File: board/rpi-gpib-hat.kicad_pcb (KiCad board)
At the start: 2 copper layers, 65 x 30 mm, 7 parts, among them J1 RPI_GPIO, J2 GPIB

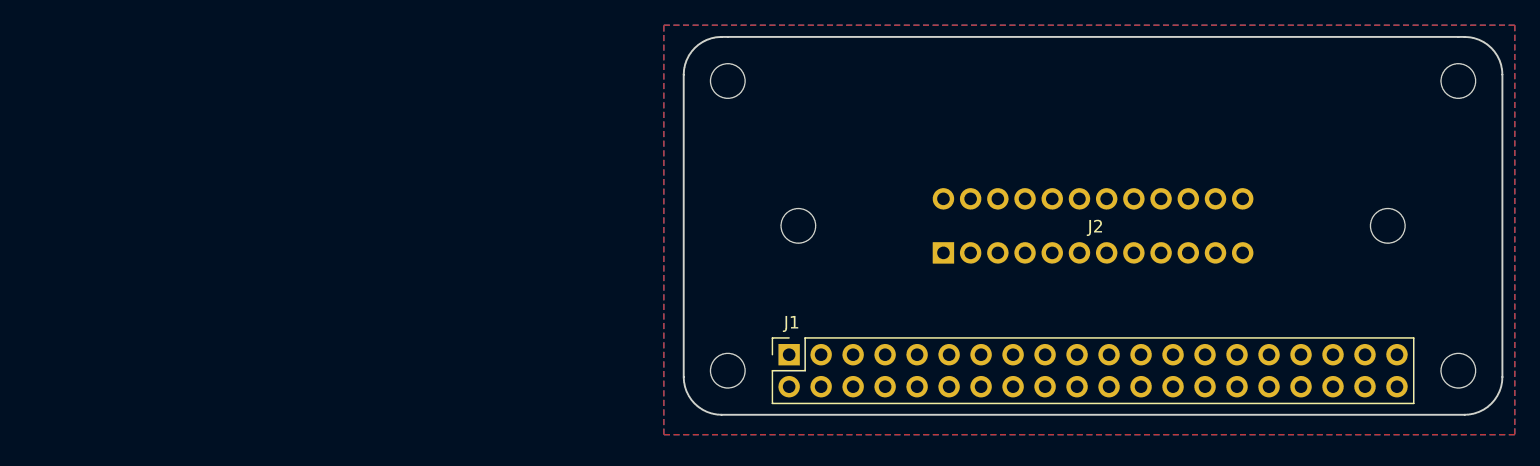
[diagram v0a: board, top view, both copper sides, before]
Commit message: Remove ground fills for now.
They're just in the way and there probably wont' be room for them.
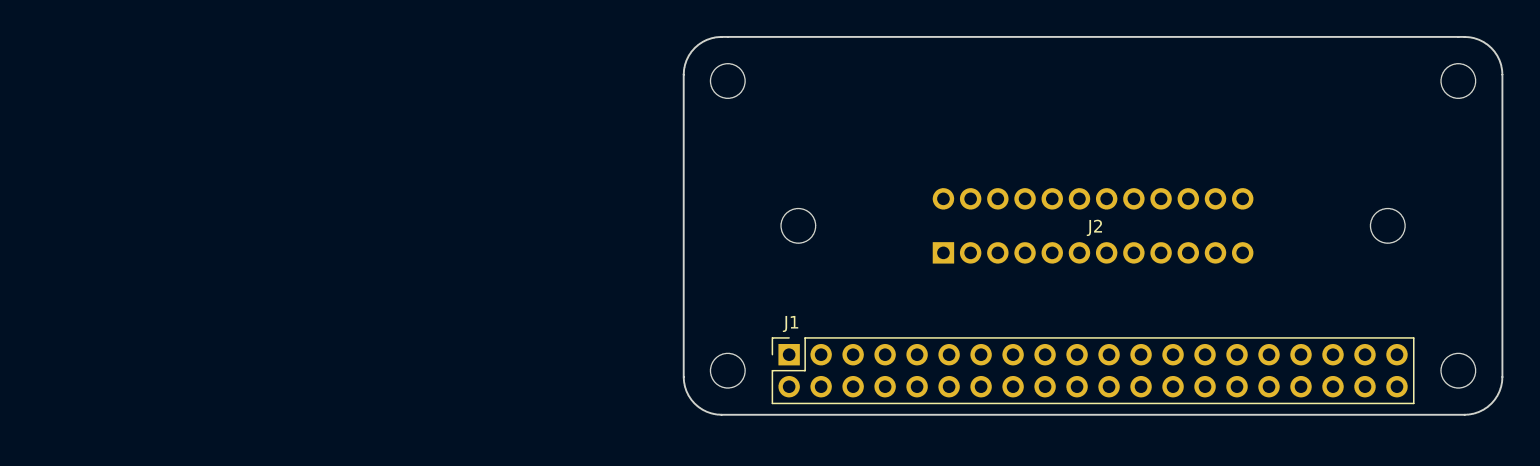
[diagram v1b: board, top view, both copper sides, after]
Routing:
- removed copper zone on B.Cu, net GND
- removed copper zone on F.Cu, net GND
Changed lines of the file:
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@@
   (gr_arc (start 158.5 123.5) (end 161.5 123.5) (angle 90) (layer Edge.Cuts) (width 0.15))
   (gr_line (start 100 96.5) (end 158 96.5) (layer Edge.Cuts) (width 0.15))
-  (zone (net 3) (net_name GND) (layer F.Cu) (hatch edge 0.508)
-    (connect_pads (clearance 0.508))
-    (min_thickness 0.254)
-    (fill yes (arc_segments 16) (thermal_gap 0.508) (thermal_bridge_width 0.508))
-    (polygon
-      (pts
-        (xy 94.92 128.08) (xy 94.92 95.568) (xy 162.484 95.568) (xy 162.484 128.08)
-      )
-    )
-  )
-  (zone (net 3) (net_name GND) (layer B.Cu) (hatch edge 0.508)
-    (connect_pads (clearance 0.508))
-    (min_thickness 0.254)
-    (fill yes (arc_segments 16) (thermal_gap 0.508) (thermal_bridge_width 0.508))
-    (polygon
-      (pts
-        (xy 94.92 128.08) (xy 94.92 95.568) (xy 162.484 95.568) (xy 162.484 128.08)
-      )
-    )
-  )
 )

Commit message: Start laying out the PCB.
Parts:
- added C1: 1u, Capacitor_SMD:C_0805_2012Metric, F.Cu at (71.8, 114.9)
- added C2: 1u, Capacitor_SMD:C_0805_2012Metric, F.Cu at (50.1, 124.9)
- added C3: 1u, Capacitor_SMD:C_0805_2012Metric, F.Cu at (58.6, 115.8)
- added D1: BAT54C, Package_TO_SOT_SMD:SOT-23, F.Cu at (98.8, 117.0)
- added D2: BAT54C, Package_TO_SOT_SMD:SOT-23, F.Cu at (98.8, 113.2)
- added D3: BAT54C, Package_TO_SOT_SMD:SOT-23, F.Cu at (98.8, 109.5)
- added D4: BAT54C, Package_TO_SOT_SMD:SOT-23, F.Cu at (98.8, 105.8)
- added D5: BAT54C, Package_TO_SOT_SMD:SOT-23, F.Cu at (45.7, 125.7)
- added D6: BAT54C, Package_TO_SOT_SMD:SOT-23, F.Cu at (54.1, 116.6)
- added D7: BAT54C, Package_TO_SOT_SMD:SOT-23, F.Cu at (71.5, 102.3)
- added D8: BAT54C, Package_TO_SOT_SMD:SOT-23, F.Cu at (54.1, 121.2)
- added R1: 3k, Resistor_SMD:R_0402_1005Metric, F.Cu at (50.1, 127.9)
- added R10: 3k, Resistor_SMD:R_0402_1005Metric, F.Cu at (80.3, 104.4)
- added R11: 3k, Resistor_SMD:R_0402_1005Metric, F.Cu at (67.4, 116.5)
- added R12: 3k, Resistor_SMD:R_0402_1005Metric, F.Cu at (63.0, 121.7)
- added R13: 3k, Resistor_SMD:R_0402_1005Metric, F.Cu at (75.9, 107.4)
- added R14: 3k, Resistor_SMD:R_0402_1005Metric, F.Cu at (75.9, 101.5)
- added R15: 3k, Resistor_SMD:R_0402_1005Metric, F.Cu at (80.3, 101.5)
- added R16: 3k, Resistor_SMD:R_0402_1005Metric, F.Cu at (54.5, 127.9)
- added R17: 6k2, Resistor_SMD:R_0402_1005Metric, F.Cu at (67.4, 113.5)
- added R18: 6k2, Resistor_SMD:R_0402_1005Metric, F.Cu at (58.6, 121.7)
- added R19: 6k2, Resistor_SMD:R_0402_1005Metric, F.Cu at (71.5, 109.0)
- added R2: 3k, Resistor_SMD:R_0402_1005Metric, F.Cu at (58.6, 118.8)
- added R20: 6k2, Resistor_SMD:R_0402_1005Metric, F.Cu at (75.9, 104.4)
- added R21: 6k2, Resistor_SMD:R_0402_1005Metric, F.Cu at (63.0, 118.8)
- added R22: 6k2, Resistor_SMD:R_0402_1005Metric, F.Cu at (58.9, 124.7)
- added R23: 6k2, Resistor_SMD:R_0402_1005Metric, F.Cu at (72.2, 120.8)
- added R24: 6k2, Resistor_SMD:R_0402_1005Metric, F.Cu at (84.7, 101.5)
- added R25: 6k2, Resistor_SMD:R_0402_1005Metric, F.Cu at (76.2, 116.2)
- added R26: 6k2, Resistor_SMD:R_0402_1005Metric, F.Cu at (67.7, 125.3)
- added R27: 6k2, Resistor_SMD:R_0402_1005Metric, F.Cu at (89.2, 104.4)
- added R28: 6k2, Resistor_SMD:R_0402_1005Metric, F.Cu at (84.7, 107.4)
- added R29: 6k2, Resistor_SMD:R_0402_1005Metric, F.Cu at (67.7, 122.4)
- added R3: 3k, Resistor_SMD:R_0402_1005Metric, F.Cu at (71.5, 106.0)
- added R30: 6k2, Resistor_SMD:R_0402_1005Metric, F.Cu at (71.8, 117.8)
- added R31: 6k2, Resistor_SMD:R_0402_1005Metric, F.Cu at (54.5, 124.9)
- added R32: 6k2, Resistor_SMD:R_0402_1005Metric, F.Cu at (80.6, 110.3)
- added R33: 500R, Resistor_SMD:R_0402_1005Metric, F.Cu at (101.8, 115.4)
- added R34: 500R, Resistor_SMD:R_0402_1005Metric, F.Cu at (101.8, 114.2)
- added R35: 500R, Resistor_SMD:R_0402_1005Metric, F.Cu at (101.8, 112.9)
- added R36: 500R, Resistor_SMD:R_0402_1005Metric, F.Cu at (101.8, 111.6)
- added R37: 500R, Resistor_SMD:R_0402_1005Metric, F.Cu at (101.8, 110.4)
- added R38: 500R, Resistor_SMD:R_0402_1005Metric, F.Cu at (101.8, 109.1)
- added R39: 500R, Resistor_SMD:R_0402_1005Metric, F.Cu at (101.8, 107.8)
- added R4: 3k, Resistor_SMD:R_0402_1005Metric, F.Cu at (67.0, 110.6)
- added R40: 500R, Resistor_SMD:R_0402_1005Metric, F.Cu at (101.8, 106.6)
- added R41: 500R, Resistor_SMD:R_0402_1005Metric, F.Cu at (85.0, 110.3)
- added R42: 500R, Resistor_SMD:R_0402_1005Metric, F.Cu at (89.1, 107.4)
- added R43: 500R, Resistor_SMD:R_0402_1005Metric, F.Cu at (72.2, 123.7)
- added R44: 500R, Resistor_SMD:R_0402_1005Metric, F.Cu at (67.7, 128.3)
- added R45: 500R, Resistor_SMD:R_0402_1005Metric, F.Cu at (76.6, 119.2)
- added R46: 500R, Resistor_SMD:R_0402_1005Metric, F.Cu at (80.6, 116.2)
- added R47: 500R, Resistor_SMD:R_0402_1005Metric, F.Cu at (85.0, 113.3)
- added R48: 500R, Resistor_SMD:R_0402_1005Metric, F.Cu at (89.4, 110.3)
- added R49: 3k9, Resistor_SMD:R_0402_1005Metric, F.Cu at (76.6, 122.1)
- added R5: 3k, Resistor_SMD:R_0402_1005Metric, F.Cu at (80.6, 113.3)
- added R50: 3k9, Resistor_SMD:R_0402_1005Metric, F.Cu at (72.2, 126.7)
- added R51: 1k, Resistor_SMD:R_0402_1005Metric, F.Cu at (81.0, 119.2)
- added R6: 3k, Resistor_SMD:R_0402_1005Metric, F.Cu at (85.0, 116.2)
- added R7: 3k, Resistor_SMD:R_0402_1005Metric, F.Cu at (63.0, 115.8)
- added R8: 3k, Resistor_SMD:R_0402_1005Metric, F.Cu at (58.9, 127.6)
- added R9: 3k, Resistor_SMD:R_0402_1005Metric, F.Cu at (71.8, 111.9)
- added TP1: TestPoint, TestPoint:TestPoint_Pad_D1.0mm, F.Cu at (88.8, 113.3)
- added U1: SN75162BDW, Package_SO:SOIC-24W_7.5x15.4mm_P1.27mm, F.Cu at (149.0, 111.0)
- added U2: SN75160BDW, Package_SO:SOIC-20W_7.5x12.8mm_P1.27mm, F.Cu at (109.0, 111.0)
- added U3: CAT24C32, Package_SO:SOIC-8_3.9x4.9mm_P1.27mm, F.Cu at (128.2, 101.5)
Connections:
- J1 pad 23: /GPIO11 -> (no net)
- J1 pad 29: /GPIO5 -> (no net)
- J1 pad 31: /GPIO6 -> (no net)
- J1 pad 36: /GPIO16 -> (no net)
- J1 pad 8: /GPIO14 -> (no net)
- J2 pad 12: Earth_Clean -> (no net)
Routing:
- net +3V3: track 0.00 -> 21.9 mm
- net /DAV: track 0.00 -> 19.9 mm, vias 0 -> 1
- net /REN: track 0.00 -> 19.7 mm
- net /EOI: track 0.00 -> 19.2 mm
- net /NRFD: track 0.00 -> 18.1 mm, vias 0 -> 1
- net /NDAC: track 0.00 -> 16.5 mm, vias 0 -> 1
- net /IFC: track 0.00 -> 15.1 mm, vias 0 -> 1
- net /DIO8: track 0.00 -> 11.1 mm
- net /DIO4: track 0.00 -> 10.8 mm
- net /DIO3: track 0.00 -> 8.85 mm
- net /SRQ: track 0.00 -> 8.54 mm
- net /DIO7: track 0.00 -> 8.42 mm
- net /DIO2: track 0.00 -> 7.46 mm
- net /ATN: track 0.00 -> 6.53 mm
- net /DIO6: track 0.00 -> 6.44 mm
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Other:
- net class Power added: clearance 0.1524, trace_width 0.3048, via_dia 0.508, via_drill 0.254

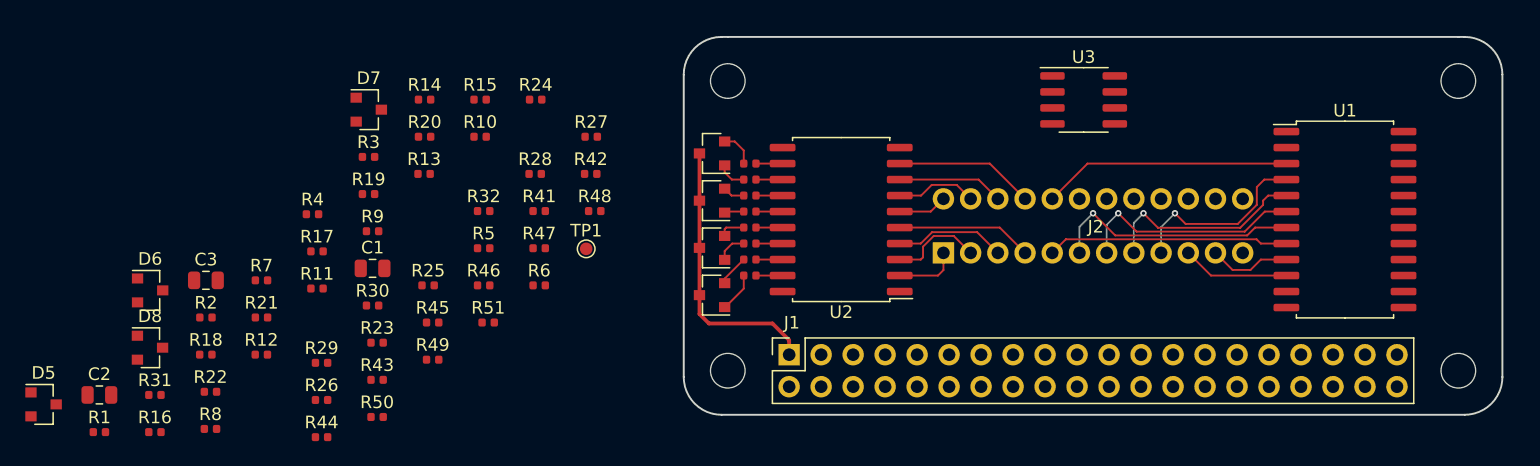
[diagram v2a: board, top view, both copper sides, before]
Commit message: Finish routing terminal-side GPIB lines.
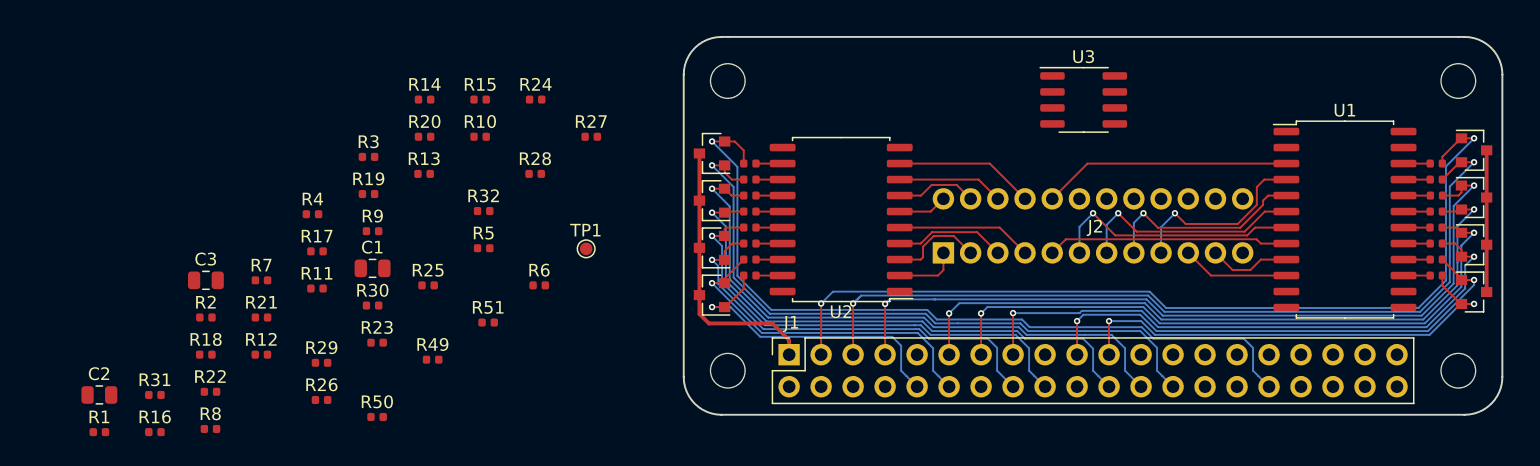
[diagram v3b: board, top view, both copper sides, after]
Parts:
- moved D5 115.4 mm to (159.2, 105.5)
- moved D6 105.4 mm to (159.2, 109.2)
- moved D8 105.2 mm to (159.2, 116.8)
- moved R44 90.3 mm to (156.2, 110.4)
- moved D7 88.4 mm to (159.2, 113.0)
- moved R43 85.4 mm to (156.3, 109.1)
- moved R45 80.0 mm to (156.2, 111.6)
- moved R46 75.7 mm to (156.2, 112.9)
- moved R41 71.3 mm to (156.2, 106.6)
- moved R47 71.2 mm to (156.2, 114.2)
- moved R42 67.1 mm to (156.2, 107.8)
- moved R48 67.0 mm to (156.2, 115.4)
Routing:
- net /GPIO2: track 0.00 -> 71.4 mm, vias 0 -> 2
- net /GPIO3: track 0.00 -> 67.0 mm, vias 0 -> 2
- net /GPIO4: track 0.00 -> 62.6 mm, vias 0 -> 2
- net /GPIO12: track 2.85 -> 62.3 mm, vias 0 -> 1
- net /GPIO17: track 0.00 -> 54.8 mm, vias 0 -> 2
- net /GPIO27: track 0.00 -> 50.8 mm, vias 0 -> 2
- net /GPIO7: track 2.30 -> 52.5 mm, vias 0 -> 1
- net /GPIO22: track 0.00 -> 47.2 mm, vias 0 -> 2
- net /GPIO8: track 1.74 -> 47.7 mm, vias 0 -> 1
- net /GPIO25: track 1.55 -> 43.3 mm, vias 0 -> 1
- net /GPIO10: track 0.00 -> 40.1 mm, vias 0 -> 2
- net /GPIO9: track 0.00 -> 37.0 mm, vias 0 -> 2
- net /GPIO24: track 2.11 -> 37.2 mm, vias 0 -> 1
- net /GPIO23: track 2.46 -> 33.4 mm, vias 0 -> 1
- net /GPIO18: track 2.50 -> 26.7 mm, vias 0 -> 1
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
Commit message: Route data bus terminators.
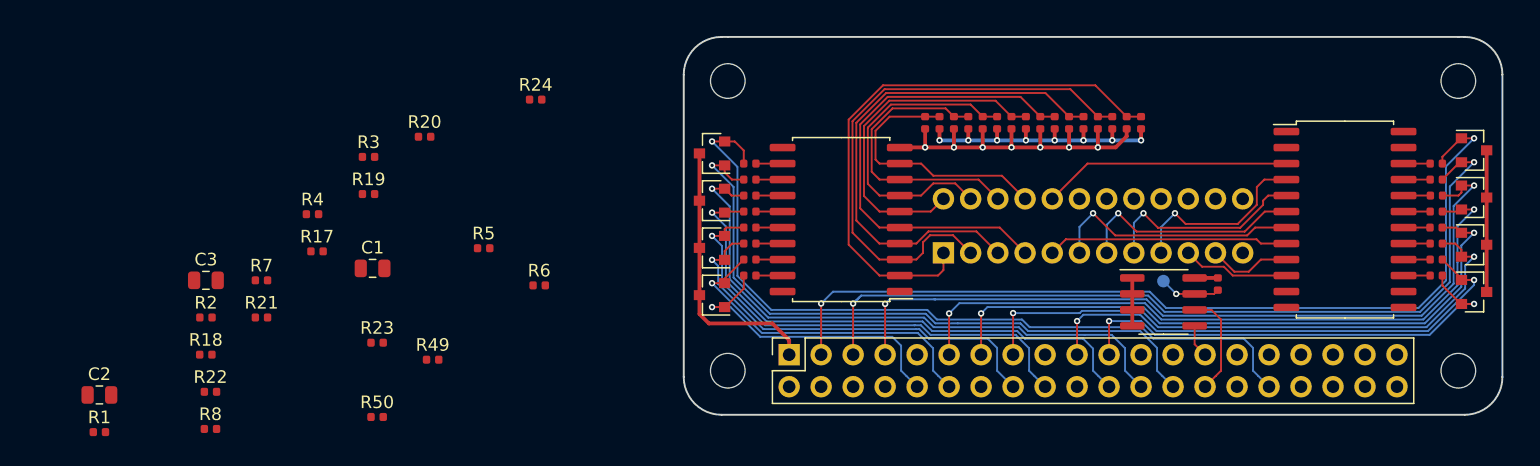
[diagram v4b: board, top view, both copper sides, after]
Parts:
- TP1: moved to B.Cu
- moved R31 67.0 mm to (118.0, 103.3), turned to 90 degrees
- moved R16 67.0 mm to (116.8, 103.3), turned to 270 degrees
- moved R12 65.6 mm to (126.0, 103.3), turned to 270 degrees
- moved R26 65.4 mm to (129.4, 103.3), turned to 90 degrees
- moved R11 62.3 mm to (128.2, 103.3), turned to 270 degrees
- moved R9 61.6 mm to (132.8, 103.3), turned to 270 degrees
- moved R51 58.0 mm to (138.9, 116.1), turned to 270 degrees
- moved R29 58.0 mm to (122.5, 103.3), turned to 90 degrees
- moved R25 56.9 mm to (131.7, 103.3), turned to 90 degrees
- moved R30 50.6 mm to (120.2, 103.3), turned to 90 degrees
- moved R10 50.2 mm to (130.5, 103.3), turned to 270 degrees
- moved R13 48.0 mm to (123.7, 103.3), turned to 270 degrees
- moved TP1 45.9 mm to (134.6, 115.9)
- moved R14 45.5 mm to (121.4, 103.3), turned to 270 degrees
- moved R28 40.3 mm to (124.8, 103.3), turned to 90 degrees
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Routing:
- net /DIO1: track 5.28 -> 45.7 mm
- net /DIO2: track 7.46 -> 43.6 mm
- net GND: track 0.00 -> 33.1 mm, vias 0 -> 7
- net /DIO3: track 8.85 -> 40.6 mm
- net /DIO4: track 10.8 -> 38.2 mm
- net +5V: track 0.00 -> 23.3 mm, vias 0 -> 8
- net /DIO5: track 3.89 -> 27.0 mm
- net /DIO6: track 6.44 -> 25.3 mm
- net /DIO7: track 8.42 -> 22.9 mm
- net /DIO8: track 11.1 -> 21.0 mm
- net /ID_SC: track 0.00 -> 8.27 mm
- net /ID_WP: track 0.00 -> 4.86 mm, vias 0 -> 1
- net /ID_SD: track 0.00 -> 2.63 mm
- net +3V3: track 33.1 -> 35.0 mm

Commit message: Route control bus terminations.
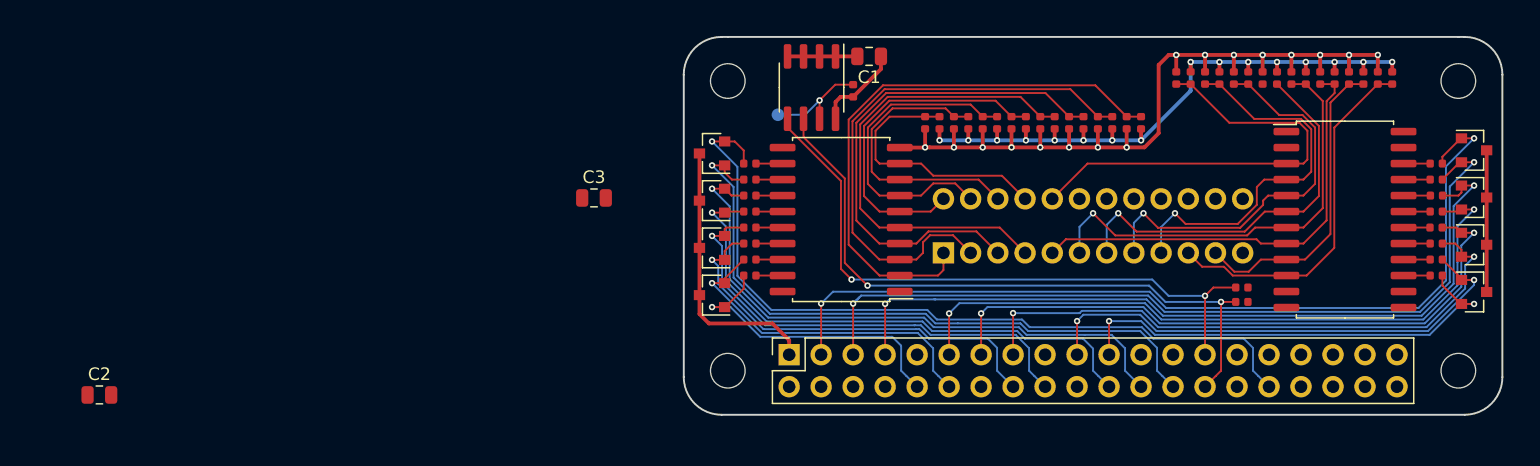
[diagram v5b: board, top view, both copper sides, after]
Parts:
- TP1: value TestPoint -> WP
- moved R8 97.9 mm to (152.7, 99.8), turned to 90 degrees
- moved R22 91.6 mm to (147.0, 99.8), turned to 270 degrees
- moved R1 91.1 mm to (136.7, 99.8), turned to 90 degrees
- moved R7 89.0 mm to (150.5, 99.8), turned to 90 degrees
- moved R21 84.0 mm to (144.7, 99.8), turned to 270 degrees
- moved R2 82.7 mm to (139.0, 99.8), turned to 90 degrees
- moved R18 82.3 mm to (137.9, 99.8), turned to 270 degrees
- moved R23 80.0 mm to (149.3, 99.8), turned to 270 degrees
- moved R4 77.3 mm to (143.6, 99.8), turned to 90 degrees
- moved R3 70.1 mm to (141.3, 99.8), turned to 90 degrees
- moved R17 69.6 mm to (135.6, 99.8), turned to 270 degrees
- moved R19 69.3 mm to (140.2, 99.8), turned to 270 degrees
- moved R50 69.3 mm to (140.8, 117.5), turned to 180 degrees
- moved R24 66.9 mm to (151.6, 99.8), turned to 270 degrees
- moved R20 66.7 mm to (142.5, 99.8), turned to 270 degrees
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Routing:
- net /ID_SD: track 2.63 -> 50.9 mm, vias 0 -> 2
- net /ID_SC: track 8.27 -> 52.6 mm, vias 0 -> 2
- net GND: track 33.1 -> 72.3 mm, vias 7 -> 16
- net +5V: track 23.3 -> 53.4 mm, vias 8 -> 16
- net /SRQ: track 8.54 -> 28.8 mm
- net /ATN: track 6.65 -> 24.6 mm
- net /EOI: track 19.2 -> 35.4 mm
- net /REN: track 19.7 -> 35.8 mm
- net /IFC: track 15.1 -> 30.6 mm
- net /DAV: track 19.9 -> 35.0 mm
- net /NDAC: track 16.5 -> 31.6 mm
- net /NRFD: track 18.1 -> 31.5 mm
- net +3V3: track 35.0 -> 40.3 mm
- net /ID_WP: track 4.86 -> 8.54 mm

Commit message: Route the rest of the board.
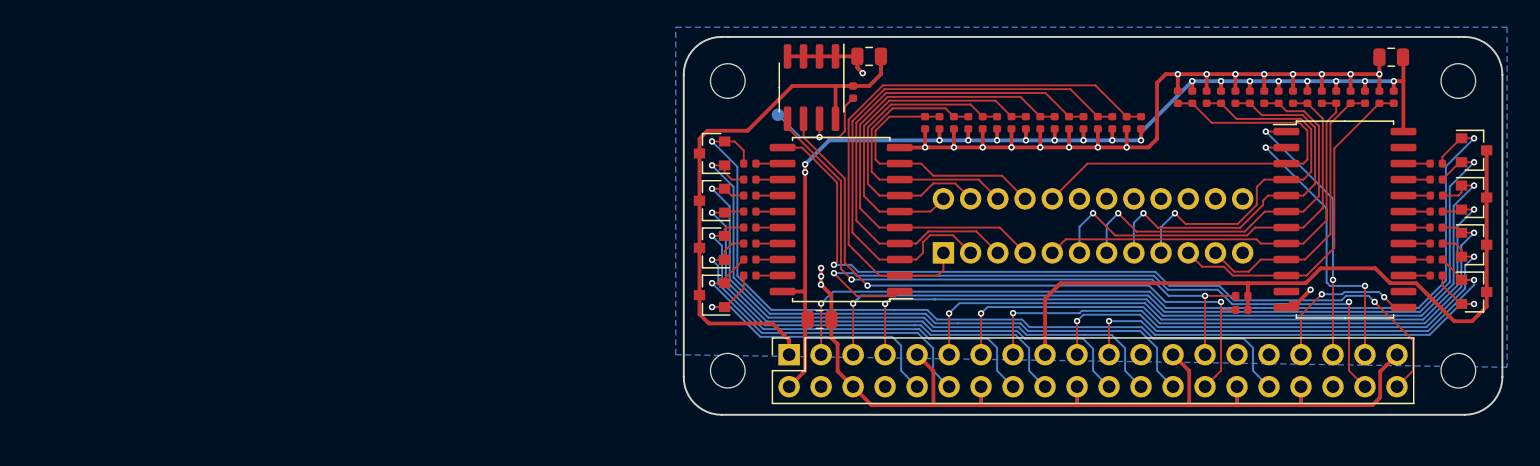
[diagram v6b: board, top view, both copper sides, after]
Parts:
- moved C2 106.0 mm to (152.7, 98.1), turned to 180 degrees
- moved C3 20.3 mm to (107.3, 118.9)
- moved R18 1.53 mm to (138.0, 101.3)
- moved R19 1.53 mm to (140.3, 101.3)
- moved R2 1.53 mm to (139.2, 101.3)
- moved R20 1.53 mm to (142.6, 101.3)
- moved R21 1.53 mm to (144.9, 101.3)
- moved R22 1.53 mm to (147.2, 101.3)
- moved R23 1.53 mm to (149.4, 101.3)
- moved R24 1.53 mm to (151.7, 101.3)
- moved R3 1.53 mm to (141.4, 101.3)
- moved R4 1.53 mm to (143.7, 101.3)
- moved R5 1.53 mm to (146.0, 101.3)
- moved R6 1.53 mm to (148.3, 101.3)
- moved R7 1.53 mm to (150.6, 101.3)
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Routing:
- net GND: track 72.3 -> 148.6 mm, vias 16 -> 21
- net /GPIO21: track 0.00 -> 65.1 mm, vias 0 -> 2
- net +3V3: track 40.3 -> 101.2 mm
- net /GPIO20: track 0.00 -> 55.4 mm, vias 0 -> 2
- net +5V: track 53.4 -> 93.4 mm, vias 16 -> 18
- net /GPIO26: track 0.00 -> 23.1 mm, vias 0 -> 2
- net /GPIO19: track 0.00 -> 22.1 mm, vias 0 -> 2
- net /GPIO13: track 0.00 -> 12.6 mm, vias 0 -> 2
- net /ID_WP: track 8.54 -> 10.6 mm
- net /DAV: track 35.0 -> 33.4 mm
- net /ATN: track 24.6 -> 23.2 mm
- net /SRQ: track 28.8 -> 27.4 mm
- net /EOI: track 35.4 -> 33.9 mm
- net /IFC: track 30.6 -> 29.9 mm
- net /NDAC: track 31.6 -> 30.8 mm
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- added copper zone on B.Cu, net GND

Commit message: Misc routing cleanup.
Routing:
- net GND: track 148.6 -> 149.2 mm
